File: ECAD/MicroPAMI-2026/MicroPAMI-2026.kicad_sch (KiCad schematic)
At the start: 20 parts, among them J1 Conn_01x05, J2 Conn_01x05, J3 MicroServo, J4 UPDI, SW3 SW_Push, U1 ATtiny3226-S, U2 ITR9608-F, U4 AMS1117-5.0, U5 ULN2803A

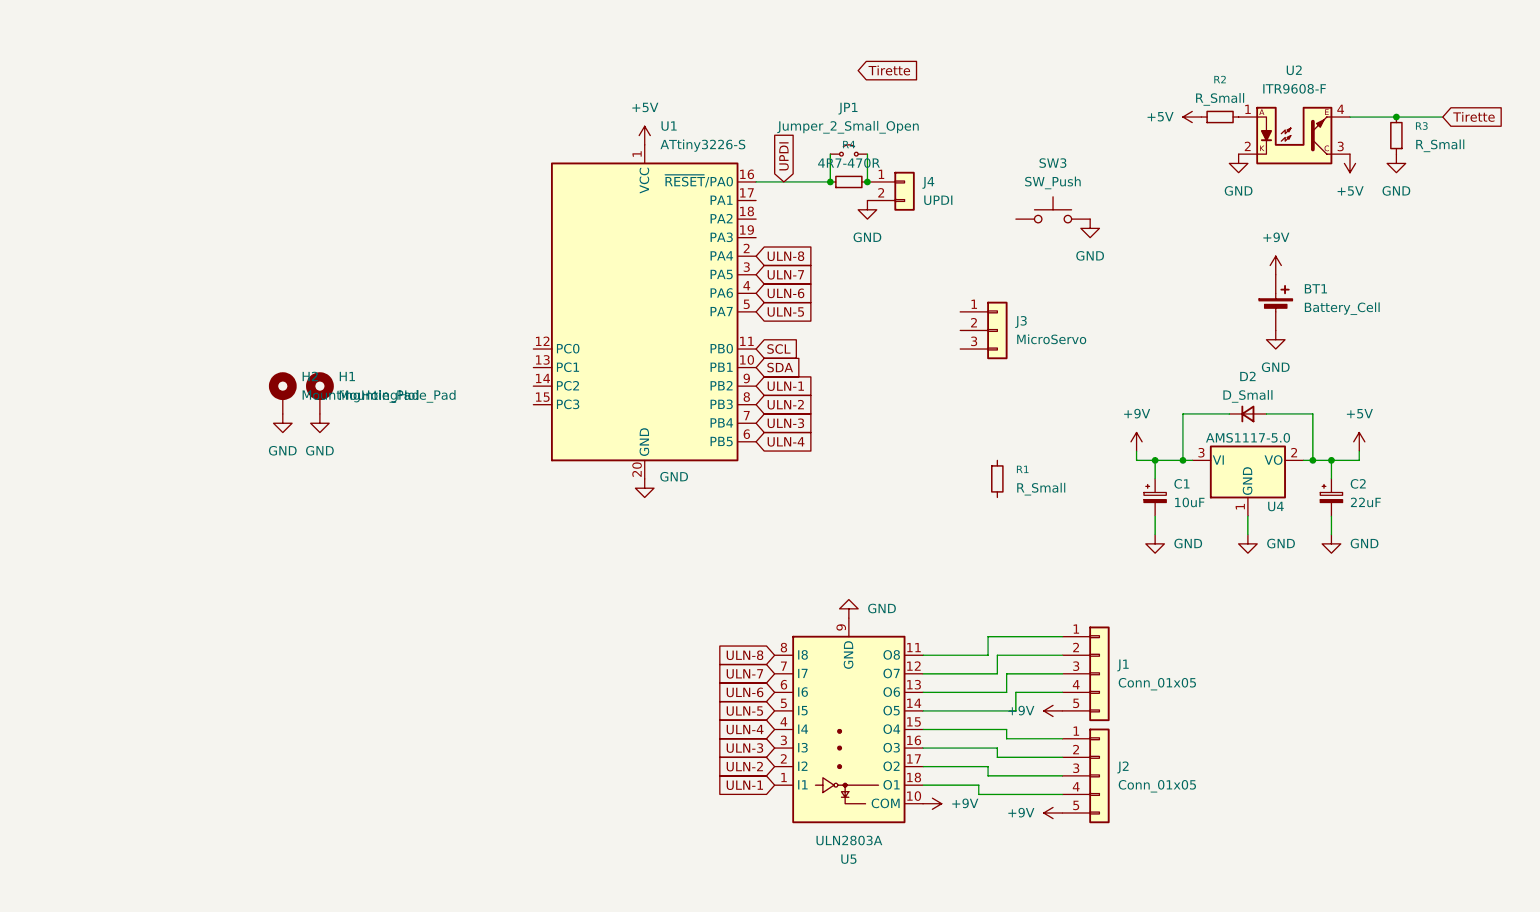
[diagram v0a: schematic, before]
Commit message: Update PCB: add resistors, change net assignments
Added R3 and R8 SMD resistors to the PCB layout and updated net assignments for several signals, including connections for Tirette, LeftSensor, and others. Replaced unconnected net labels with specific net names for improved clarity. Updated backup files and made minor changes to project and cache files.
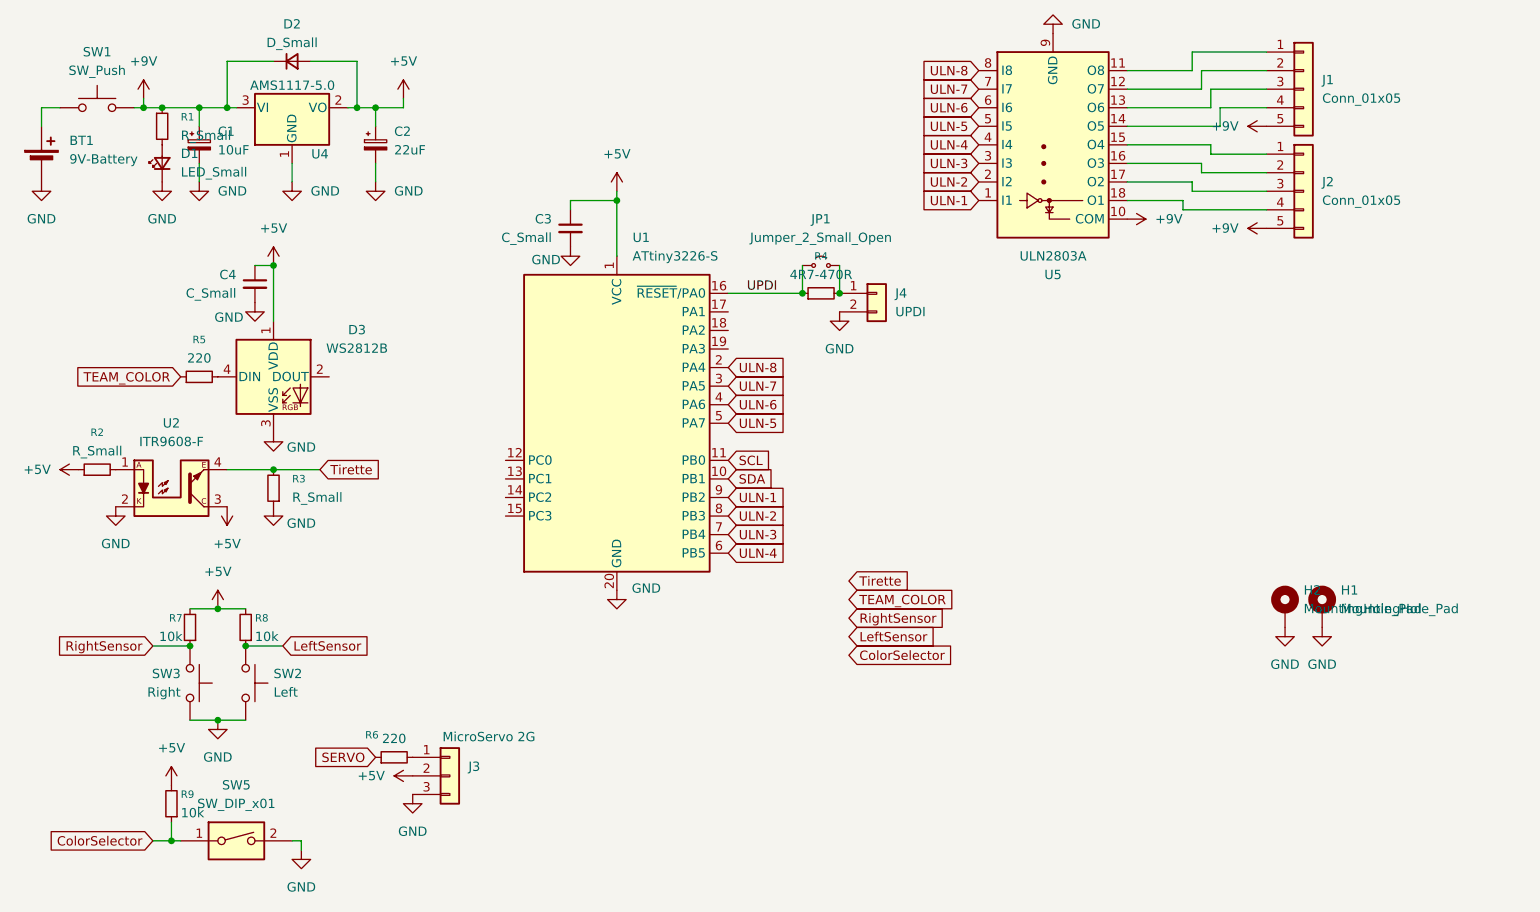
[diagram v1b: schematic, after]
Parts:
- added C3, C4: C_Small, Capacitor_SMD:C_1206_3216Metric_Pad1.33x1.80mm_HandSolder, symbol Device:C_Small
- added D1: LED_Small, LED_SMD:LED_1206_3216Metric_Pad1.42x1.75mm_HandSolder, symbol Device:LED_Small
- added D3: WS2812B, LED_SMD:LED_WS2812B_PLCC4_5.0x5.0mm_P3.2mm, symbol LED:WS2812B
- added R5, R6: 220, Resistor_SMD:R_1206_3216Metric_Pad1.30x1.75mm_HandSolder, symbol Device:R_Small
- added R7, R8, R9: 10k, Resistor_SMD:R_1206_3216Metric_Pad1.30x1.75mm_HandSolder, symbol Device:R_Small
- added SW1: SW_Push, Connector_Molex:Molex_KK-254_AE-6410-02A_1x02_P2.54mm_Vertical, symbol Switch:SW_Push
- added SW2: Left, Button_Switch_THT:SW_XKB_DM1-16UP-1, symbol Switch:SW_Push
- added SW5: SW_DIP_x01, Button_Switch_THT:SW_DIP_SPSTx01_Slide_9.78x4.72mm_W7.62mm_P2.54mm, symbol Switch:SW_DIP_x01
- BT1: value Battery_Cell -> 9V-Battery
- J3: value MicroServo -> MicroServo 2G; footprint (none) -> Connector_PinHeader_2.54mm:PinHeader_1x03_P2.54mm_Vertical
- J4: footprint (none) -> Connector_PinHeader_2.54mm:PinHeader_1x02_P2.54mm_Horizontal
- JP1: footprint (none) -> Jumper:SolderJumper-2_P1.3mm_Open_RoundedPad1.0x1.5mm
- SW3: value SW_Push -> Right
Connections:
- net +5V: now also J3.2 (Pin_2), C3.1, C4.1, D3.1 (VDD), R7.2, R8.2, R9.2
- net +9V: now also R1.1, SW1.2; no longer BT1.1 (+)
- net GND: now also J3.3 (Pin_3), C3.2, C4.2, D1.1 (K), D3.3 (VSS), SW2.2, SW5.2
- net at R1.2: now also D1.2 (A)
- net at J3.1 (Pin_1): now also R6.2
- net RightSensor: now reaches SW3.1
- net RightSensor: now also R7.1
- new net: D3.4 (DIN), R5.2
- new net: BT1.1 (+), SW1.1
- new net ColorSelector: R9.1, SW5.1
- new net LeftSensor: R8.1, SW2.1
- new net SERVO: R6.1
- new net TEAM_COLOR: R5.1
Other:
- moved on the sheet: BT1, C1, C2, D2, H1, H2, J1, J2, J3, J4, JP1, R1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

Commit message: Board routing
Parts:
- removed J4: UPDI, Connector_PinHeader_2.54mm:PinHeader_1x02_P2.54mm_Horizontal, symbol Connector_Generic:Conn_01x02
- added D5: SS14, Diode_SMD:D_SMA_Handsoldering, symbol Device:D_Schottky_Small
- added J5: UPDI, Connector_PinHeader_2.54mm:PinHeader_1x03_P2.54mm_Vertical, symbol Connector_Generic:Conn_01x03
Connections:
- net +5V: now also D5.1 (K)
- net ColorSelector: now also U1.14 (PC2)
- net GND: now also J5.3 (Pin_3)
- net LeftSensor: now also U1.19 (PA3)
- net RightSensor: now also U1.18 (PA2)
- net SERVO: now also U1.12 (PC0)
- net TEAM_COLOR: now also U1.13 (PC1)
- net Tirette: now also U1.15 (PC3)
- net +BATT: now reaches BT1.1 (+), SW1.1
- net at JP1.2 (B), R4.2: now also J5.1 (Pin_1)
- new net: D5.2 (A), J5.2 (Pin_2)
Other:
- moved on the sheet: R4

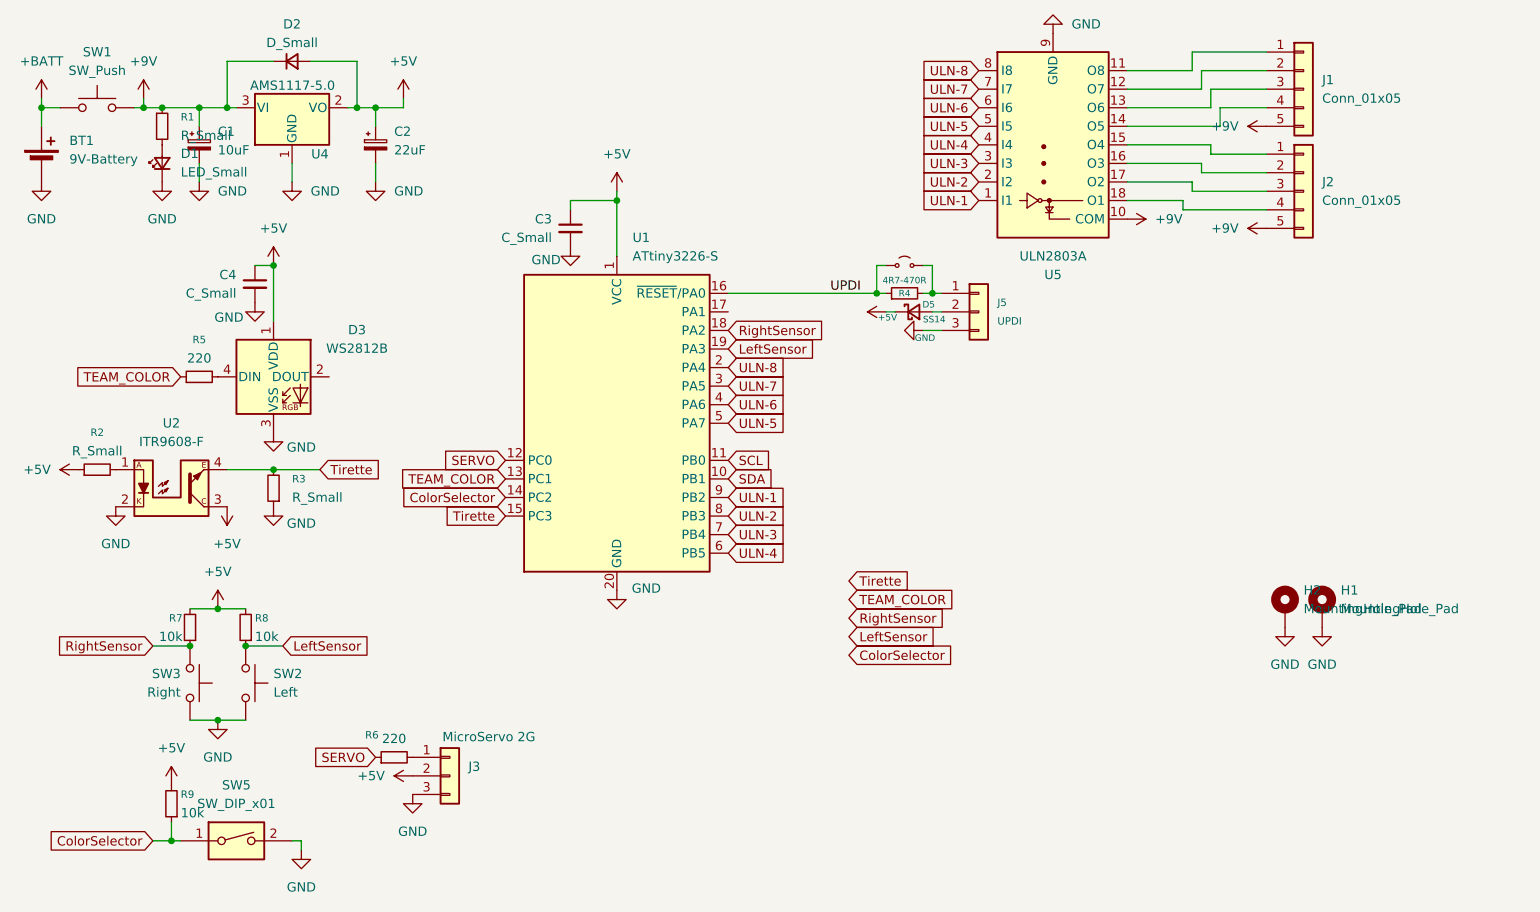
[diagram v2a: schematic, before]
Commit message: update BAU - add oled
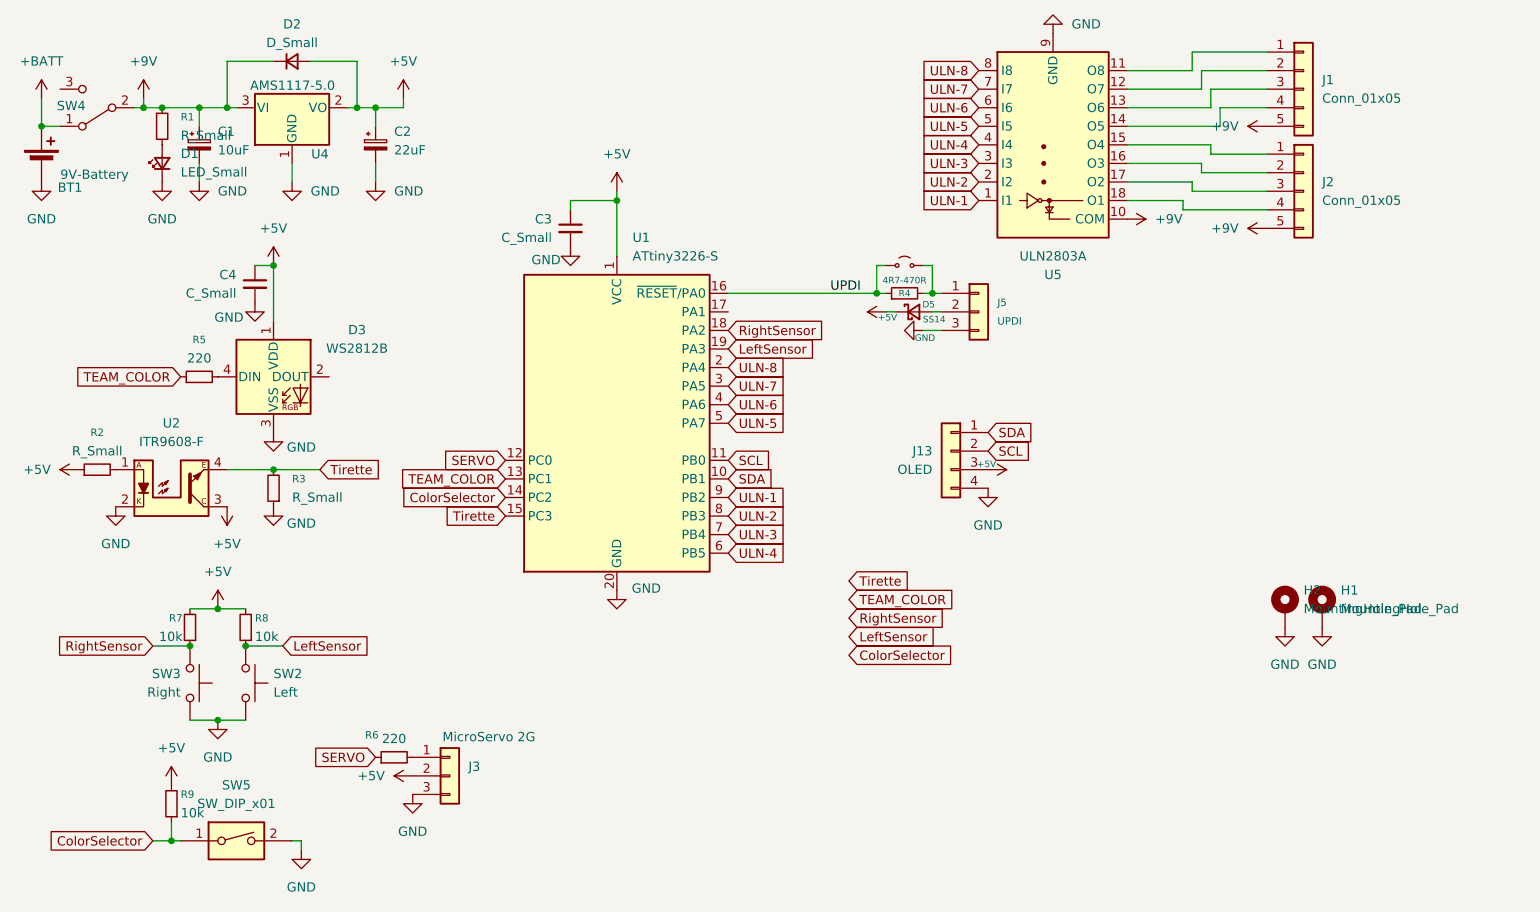
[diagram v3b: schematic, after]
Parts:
- removed SW1: SW_Push, Connector_Molex:Molex_KK-254_AE-6410-02A_1x02_P2.54mm_Vertical, symbol Switch:SW_Push
- added J13: OLED, Connector_PinSocket_2.54mm:PinSocket_1x04_P2.54mm_Vertical, symbol Connector_Generic:Conn_01x04
- added SW4: SW_SPDT, Switch:SK-12D10 1P2T, symbol Switch:SW_SPDT
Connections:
- net +5V: now also J13.3 (Pin_3)
- net +9V: now also SW4.2 (B)
- net +BATT: now also SW4.1 (A)
- net GND: now also J13.4 (Pin_4)
- net SCL: now also J13.2 (Pin_2)
- net SDA: now also J13.1 (Pin_1)

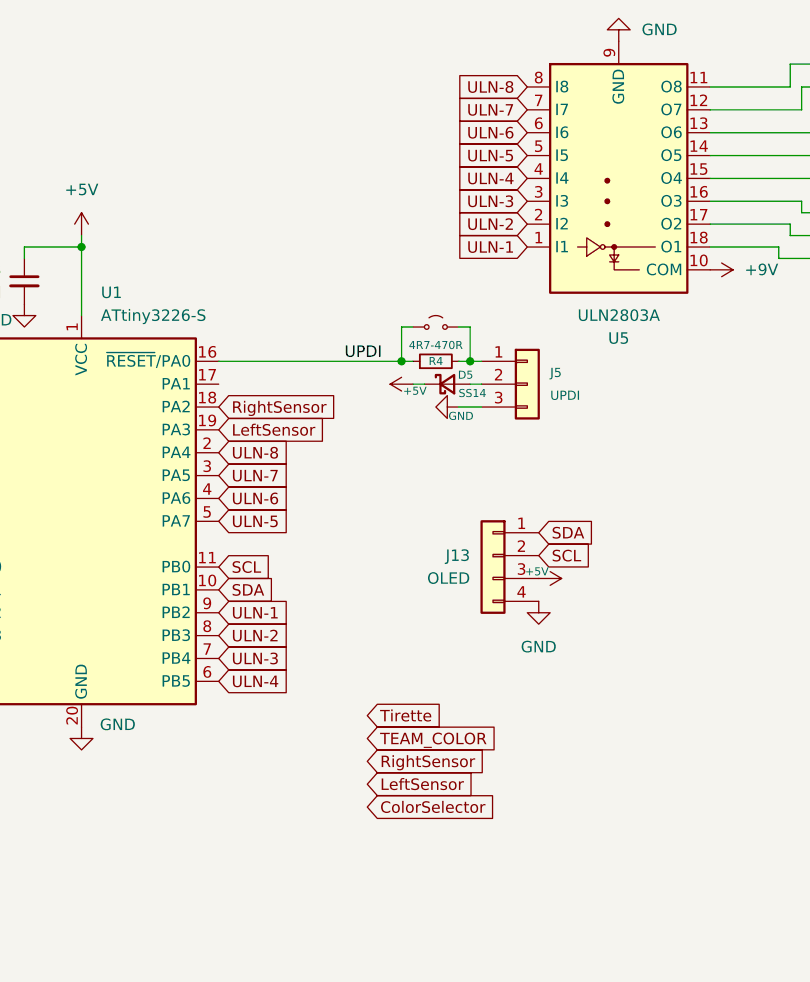
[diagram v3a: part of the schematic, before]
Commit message: add a robot selector jumper
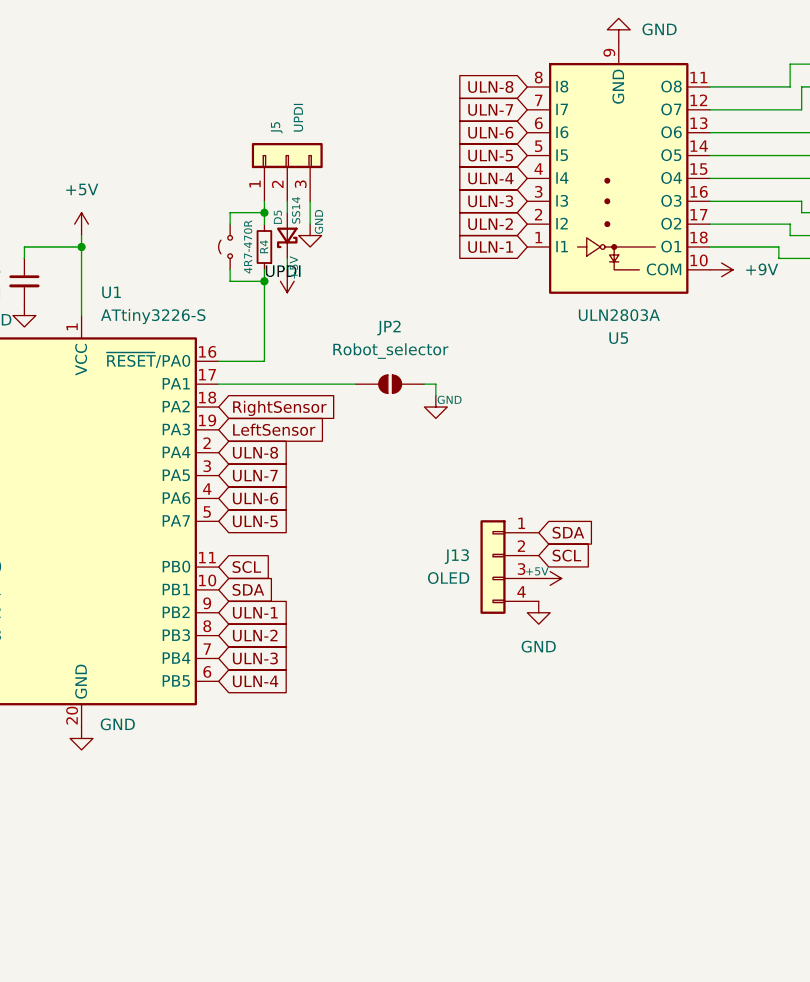
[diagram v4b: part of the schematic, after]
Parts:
- added JP2: Robot_selector, Jumper:SolderJumper-2_P1.3mm_Open_RoundedPad1.0x1.5mm, symbol Jumper:SolderJumper_2_Open
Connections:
- net GND: now also JP2.2 (B)
- net at U1.17 (PA1): now also JP2.1 (A)
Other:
- moved on the sheet: D5, J5, R4

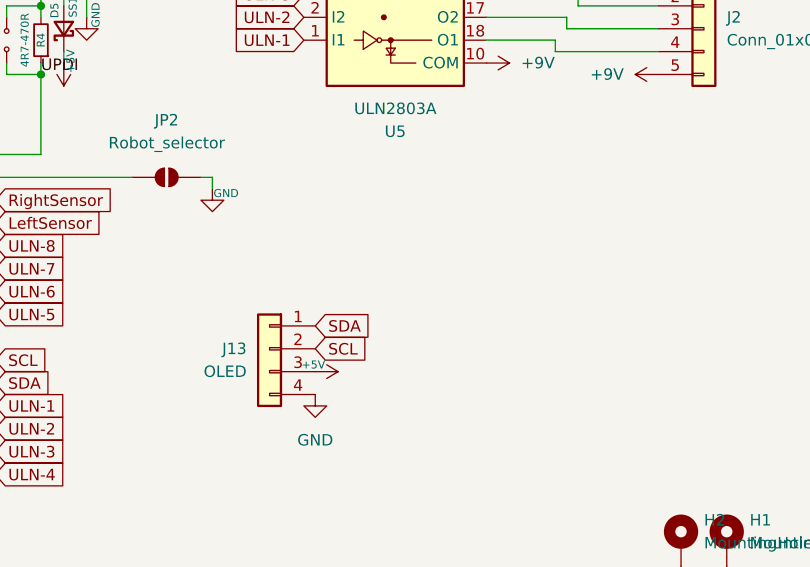
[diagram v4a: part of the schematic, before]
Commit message: add I2C resistor
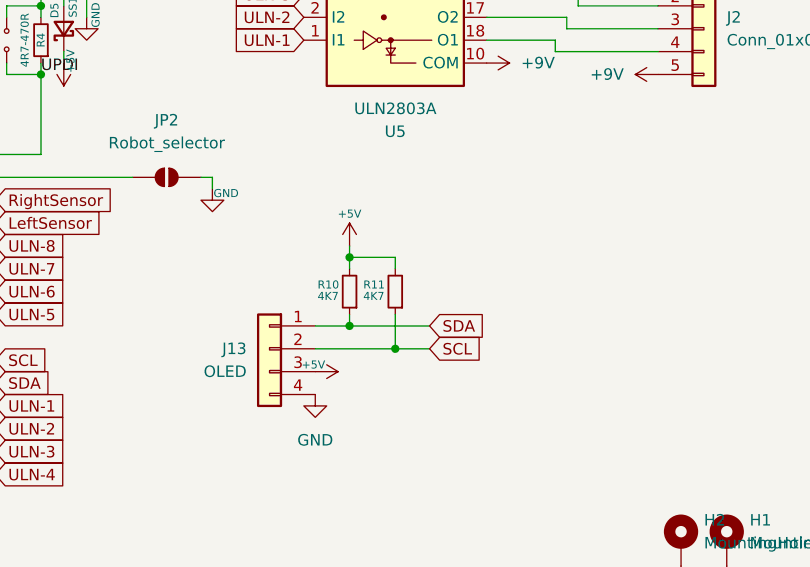
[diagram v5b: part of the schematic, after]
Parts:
- added R10, R11: 4K7, Resistor_SMD:R_1206_3216Metric_Pad1.30x1.75mm_HandSolder, symbol Device:R_Small
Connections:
- net +5V: now also R10.2, R11.2
- net SCL: now also R11.1
- net SDA: now also R10.1
